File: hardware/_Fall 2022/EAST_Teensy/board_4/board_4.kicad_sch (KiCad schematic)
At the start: 7 parts, among them J1 Conn_01x04, J2 Conn_02x10_Counter_Clockwise, U1 Teensy4.1

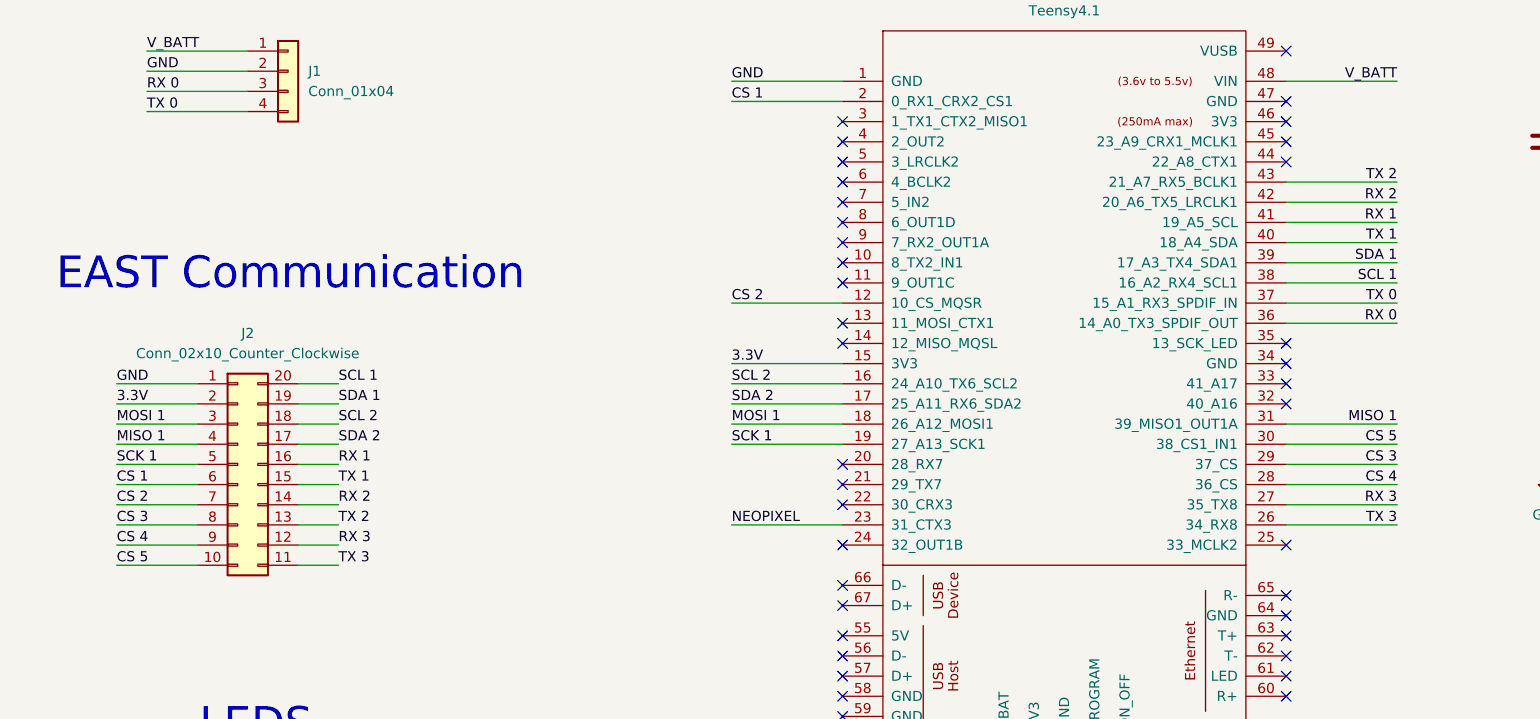
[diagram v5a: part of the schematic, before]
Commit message: Update pin connections
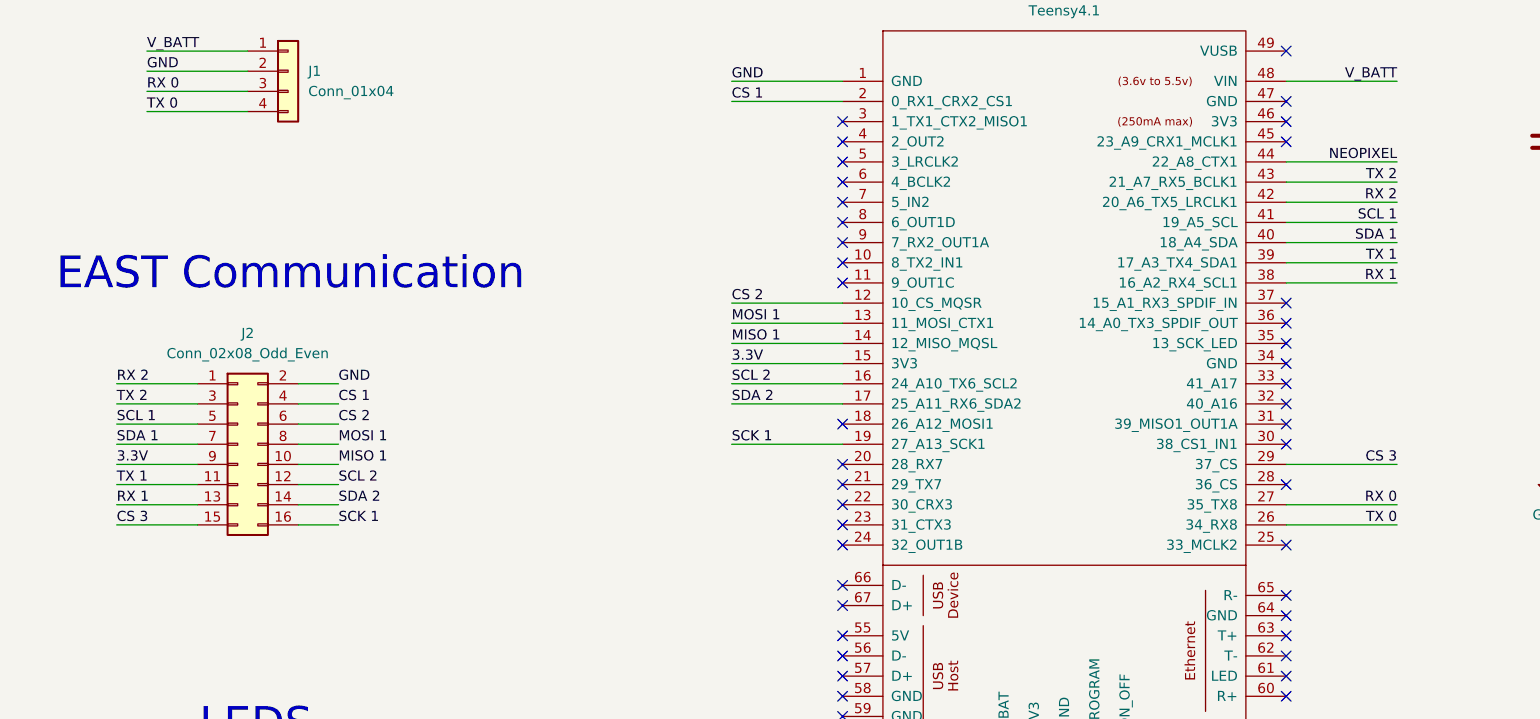
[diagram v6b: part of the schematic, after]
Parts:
- removed J2: Conn_02x10_Counter_Clockwise, Connector_PinHeader_2.54mm:PinHeader_2x10_P2.54mm_Vertical, symbol Connector_Generic:Conn_02x10_Counter_Clockwise
- added J2: Conn_02x08_Odd_Even, Connector_PinHeader_2.54mm:PinHeader_2x08_P2.54mm_Vertical, symbol Connector_Generic:Conn_02x08_Odd_Even
- C2: footprint Capacitor_Tantalum_SMD:CP_EIA-1608-08_AVX-J -> Capacitor_SMD:C_0201_0603Metric
- D1, D2: footprint neopixel:LED_1655 -> Neopixel:LED_1655
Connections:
- net RX 3 is gone; now on net RX 0: U1.27 (35_TX8)
- net TX 3 is gone; now on net TX 0: U1.26 (34_RX8)
- net 3.3V: now also J2.9 (Pin_9)
- net CS 1: now also J2.4 (Pin_4)
- net CS 2: now also J2.6 (Pin_6)
- net CS 3: now also J2.15 (Pin_15)
- net GND: now also J2.2 (Pin_2)
- net MISO 1: now also U1.14 (12_MISO_MQSL), J2.10 (Pin_10); no longer U1.31 (39_MISO1_OUT1A)
- net MOSI 1: now also U1.13 (11_MOSI_CTX1), J2.8 (Pin_8); no longer U1.18 (26_A12_MOSI1)
- net NEOPIXEL: now also U1.44 (22_A8_CTX1); no longer U1.23 (31_CTX3)
- net RX 0: no longer U1.36 (14_A0_TX3_SPDIF_OUT)
- net RX 1: now also U1.38 (16_A2_RX4_SCL1), J2.13 (Pin_13); no longer U1.41 (19_A5_SCL)
- net RX 2: now also J2.1 (Pin_1)
- net SCK 1: now also J2.16 (Pin_16)
- net SCL 1: now also U1.41 (19_A5_SCL), J2.5 (Pin_5); no longer U1.38 (16_A2_RX4_SCL1)
- net SCL 2: now also J2.12 (Pin_12)
- net SDA 1: now also U1.40 (18_A4_SDA), J2.7 (Pin_7); no longer U1.39 (17_A3_TX4_SDA1)
- net SDA 2: now also J2.14 (Pin_14)
- net TX 0: no longer U1.37 (15_A1_RX3_SPDIF_IN)
- net TX 1: now also U1.39 (17_A3_TX4_SDA1), J2.11 (Pin_11); no longer U1.40 (18_A4_SDA)
- net TX 2: now also J2.3 (Pin_3)
- net CS 4: no longer names the net of U1.28 (36_CS)
- net CS 5: no longer names the net of U1.30 (38_CS1_IN1)
- no-connect marks 43 -> 47

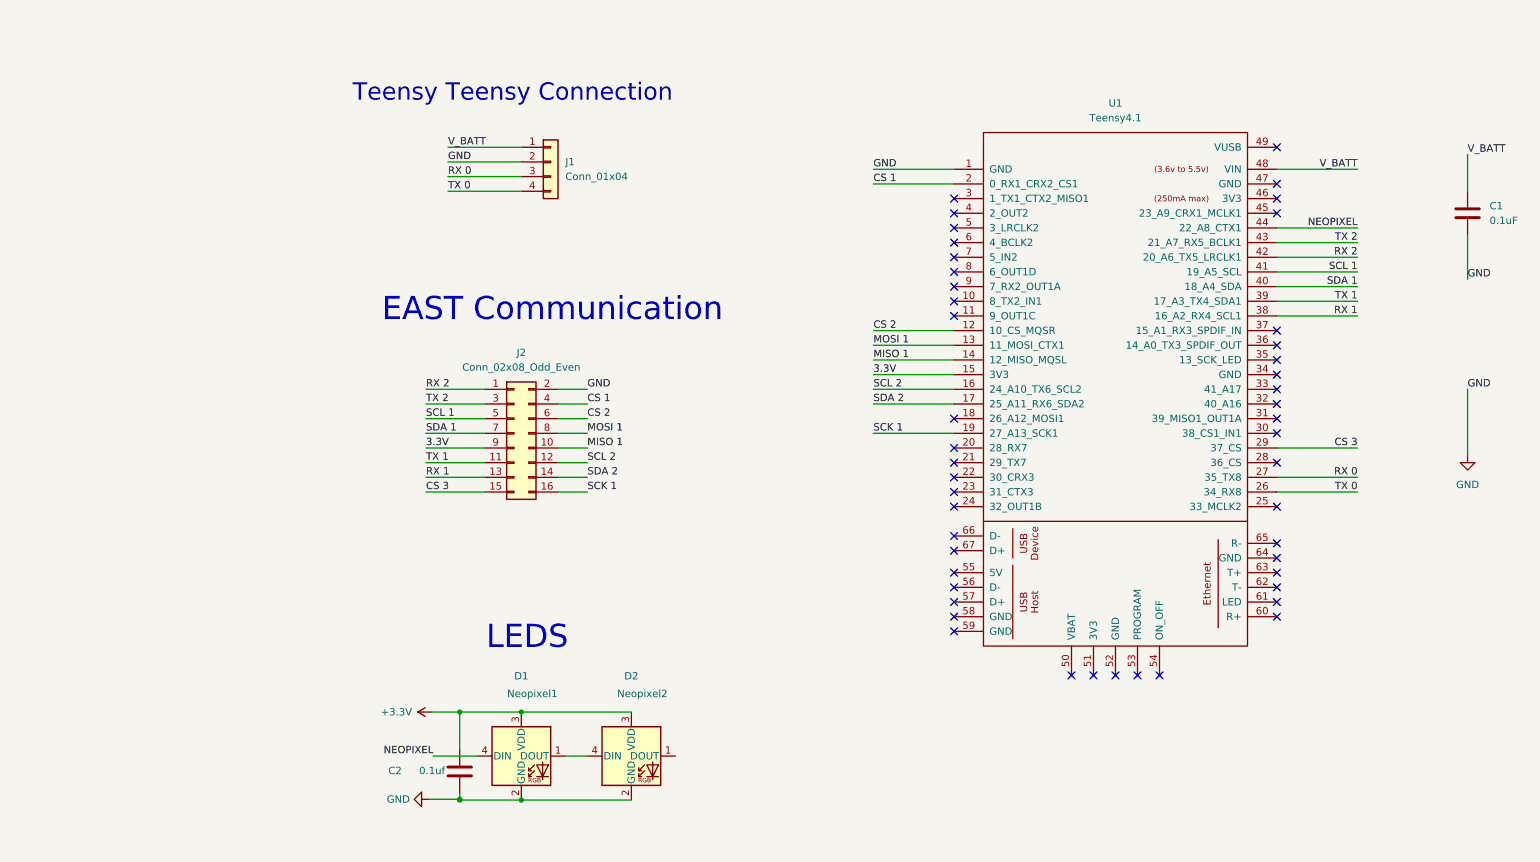
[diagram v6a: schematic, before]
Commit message: reorganize shematic
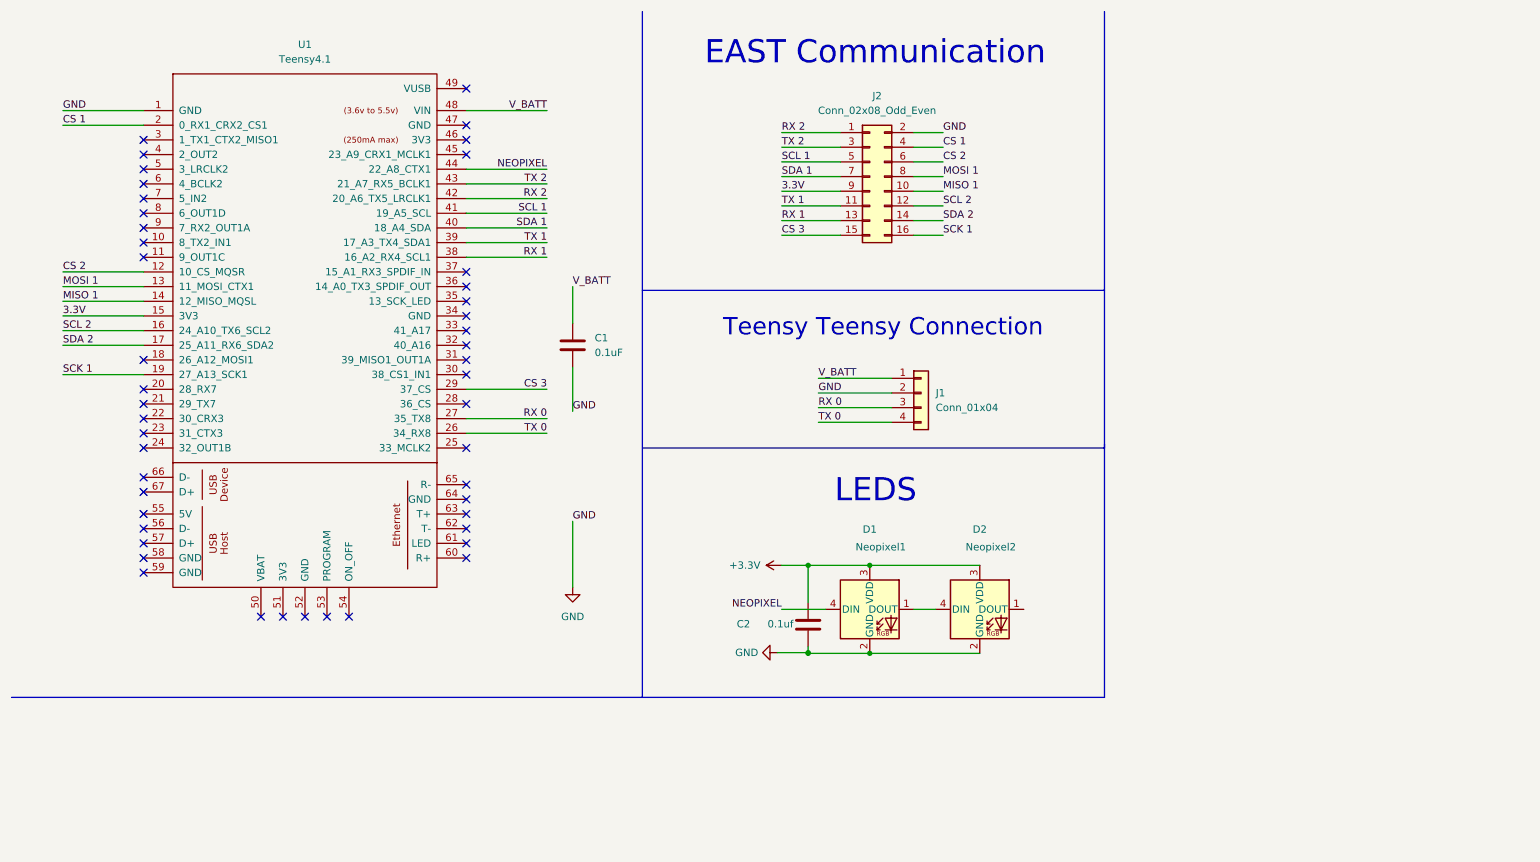
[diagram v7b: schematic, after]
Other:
- moved on the sheet: C1, C2, D1, D2, J1, J2, U1

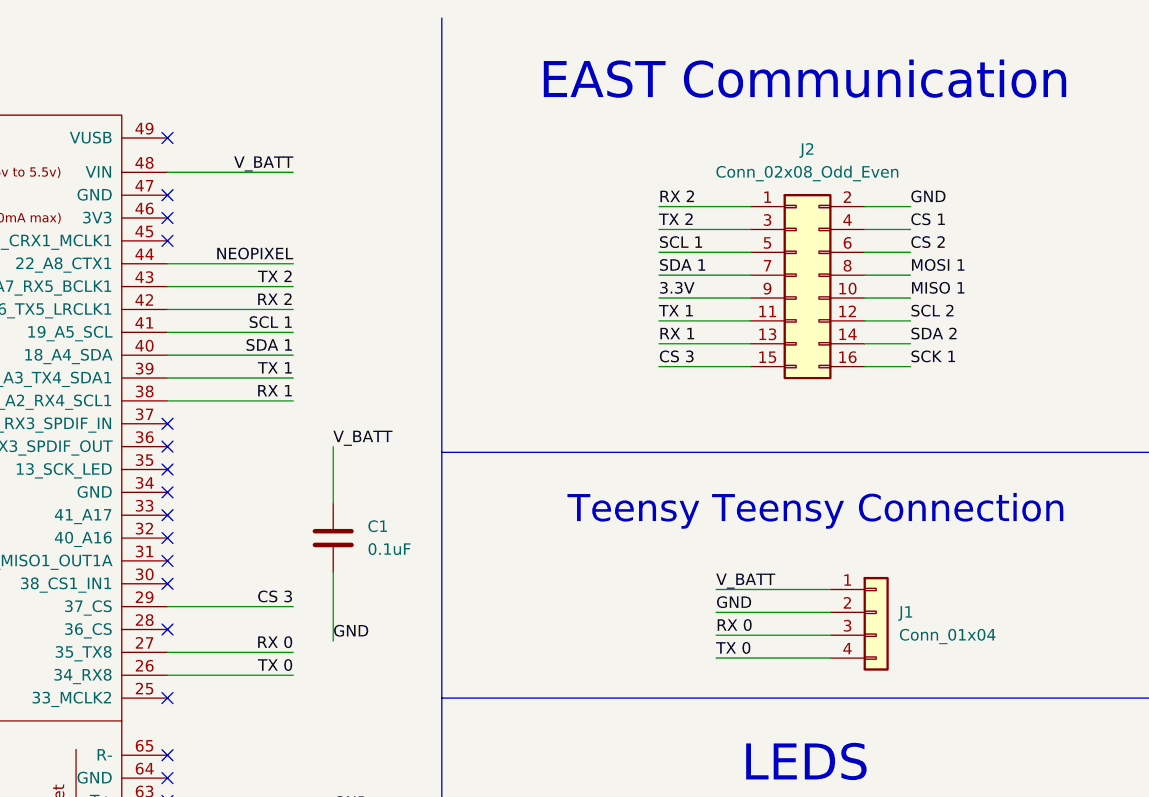
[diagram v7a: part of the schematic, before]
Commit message: Update EAST connectors
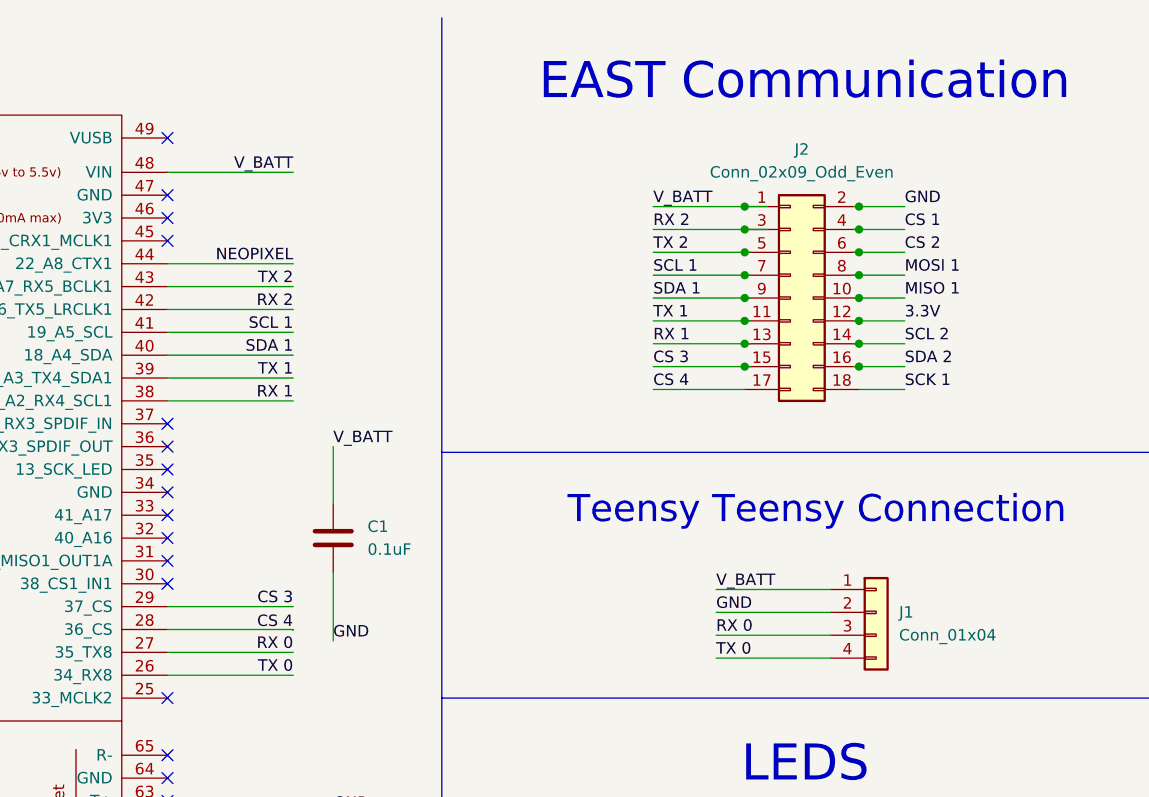
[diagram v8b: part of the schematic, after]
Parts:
- removed J2: Conn_02x08_Odd_Even, Connector_PinHeader_2.54mm:PinHeader_2x08_P2.54mm_Vertical, symbol Connector_Generic:Conn_02x08_Odd_Even
- added J2: Conn_02x09_Odd_Even, Connector_PinHeader_2.54mm:PinHeader_2x09_P2.54mm_Vertical, symbol Connector_Generic:Conn_02x09_Odd_Even
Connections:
- net 3.3V: now also J2.12 (Pin_12)
- net CS 1: now also J2.4 (Pin_4)
- net CS 2: now also J2.6 (Pin_6)
- net CS 3: now also J2.15 (Pin_15)
- net GND: now also J2.2 (Pin_2)
- net MISO 1: now also J2.10 (Pin_10)
- net MOSI 1: now also J2.8 (Pin_8)
- net RX 1: now also J2.13 (Pin_13)
- net RX 2: now also J2.3 (Pin_3)
- net SCK 1: now also J2.18 (Pin_18)
- net SCL 1: now also J2.7 (Pin_7)
- net SCL 2: now also J2.14 (Pin_14)
- net SDA 1: now also J2.9 (Pin_9)
- net SDA 2: now also J2.16 (Pin_16)
- net TX 1: now also J2.11 (Pin_11)
- net TX 2: now also J2.5 (Pin_5)
- net V_BATT: now also J2.1 (Pin_1)
- net CS 4: now reaches U1.28 (36_CS)
- net CS 4: now also J2.17 (Pin_17)
- no-connect marks 47 -> 46
